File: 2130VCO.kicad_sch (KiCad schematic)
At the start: 0 parts

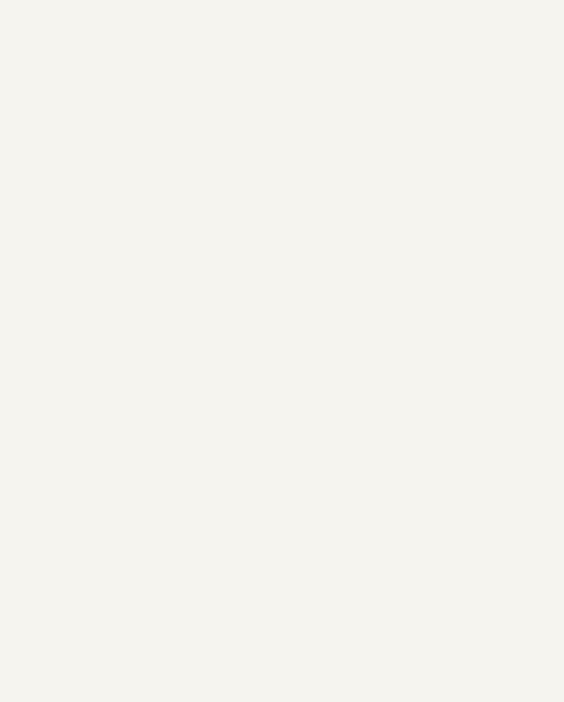
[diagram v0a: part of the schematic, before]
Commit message: added switchschematic
added switch schematidc with STMMicrocontroller and analog switches
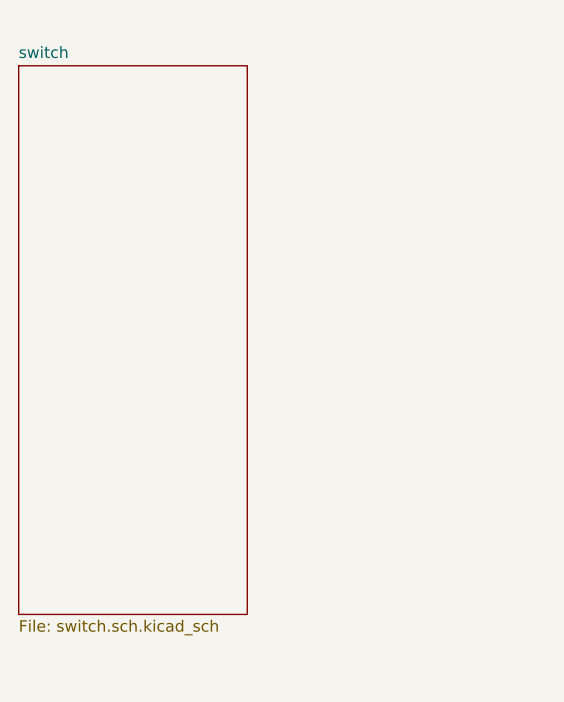
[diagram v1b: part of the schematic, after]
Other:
- added sheet switch (switch.sch.kicad_sch)
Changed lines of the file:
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@@
 	(paper "A4")
+	(sheet
+		(at 27.94 60.96)
+		(size 25.4 60.96)
+		(fields_autoplaced yes)
+		(stroke
+			(width 0.1524)
+			(type solid)
+		)
+		(fill
+			(color 0 0 0 0.0000)
+		)
+		(property "Sheetname" "switch"
+			(at 27.94 60.2484 0)
+			(effects
+				(font
+					(size 1.27 1.27)
+				)
+				(justify left bottom)
+			)
+		)
+		(property "Sheetfile" "switch.sch.kicad_sch"
+			(at 27.94 122.5046 0)
+			(effects
+				(font
+					(size 1.27 1.27)
+				)
+				(justify left top)
+			)
+		)
+		(instances
+			(project "2130VCO"
+				(path "/4b76d7ba-2e9a-48ca-9682-f8dc31b1b3ae"
+					(page "4")
+				)
+			)
+		)
+	)
 	(sheet
 		(at 205.74 93.98)
